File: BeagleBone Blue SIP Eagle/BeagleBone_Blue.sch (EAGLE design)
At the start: 278 parts, among them M1 JST_ZH_2, M2 JST_ZH_2, M3 JST_ZH_2, M4 JST_ZH_2, P10 SCHA5B0200, Q3 MOSFET-N, U1 TPD4S012_DRY_6, U4 TPD4S012_DRY_6, U5 24LC_32AT-I/OT, U6 SN74LVC1G07_DCK_5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

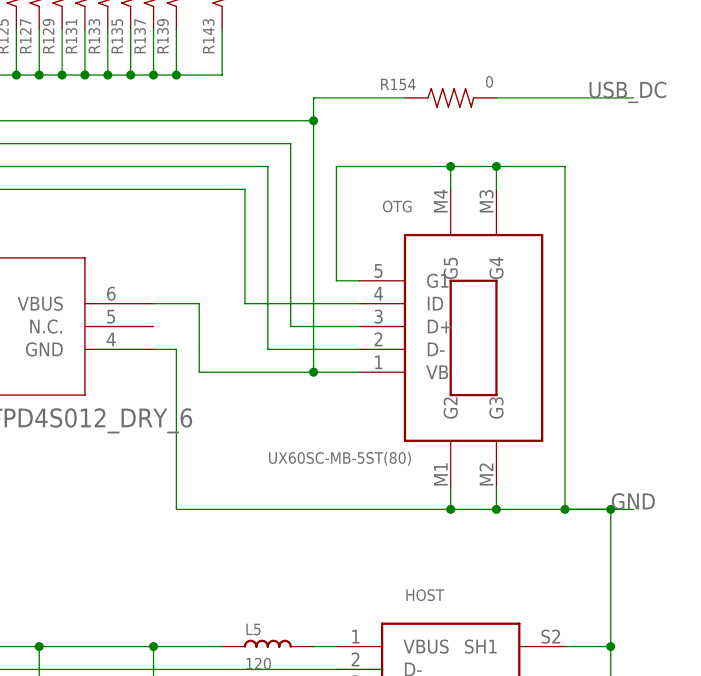
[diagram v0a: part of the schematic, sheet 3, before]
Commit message: swap to MicroUSB connector
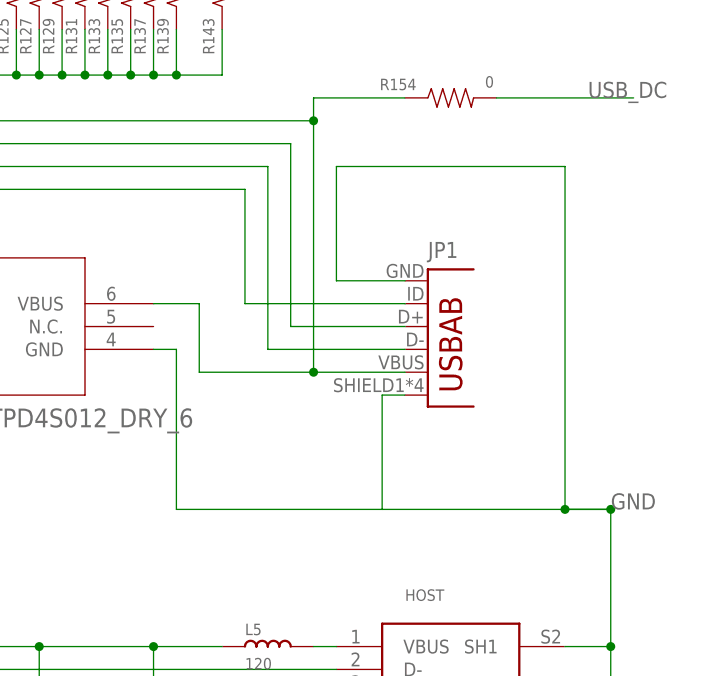
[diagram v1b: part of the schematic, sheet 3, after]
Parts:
- removed OTG: UX60SC-MB-5ST(80), BeagleBone_Blue:UX60SC-MB-5ST(80)
- added JP1: (no value), Strawson_Eagle_Lib:USB-AB
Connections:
- net GND: now also JP1.GND, JP1.SHIELD; no longer OTG.G1, OTG.G2, OTG.G3, OTG.G4, OTG.G5
- net N$117: now also JP1.D+; no longer OTG.D+
- net N$118: now also JP1.D-; no longer OTG.D-
- net N$119: now also JP1.USBID; no longer OTG.ID
- net USB0_VBUS: now also JP1.VBUS; no longer OTG.VB
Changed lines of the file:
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@@
 <part name="U4" library="BeagleBone_Blue" deviceset="TPD4S012_DRY_6" device=""/>
 <part name="U7" library="BeagleBone_Blue" deviceset="TPS2051B_D_8" device=""/>
-<part name="OTG" library="BeagleBone_Blue" deviceset="UX60SC-MB-5ST(80)" device=""/>
 <part name="HOST" library="BeagleBone_Blue" deviceset="87520-0010BLF" device=""/>
 <part name="R149" library="Strawson_Eagle_Lib" deviceset="RESISTOR" device="0402-RES" value="0"/>
@@
 <part name="R158" library="Strawson_Eagle_Lib" deviceset="RESISTOR" device="0402-RES" value="10K,1%"/>
 <part name="5VREG" library="BeagleBone_Blue" deviceset="AP1509" device="SOIC-8-TIGHT" value="AP1509SOIC-8-TIGHT"/>
+<part name="JP1" library="Strawson_Eagle_Lib" deviceset="USB-AB" device=""/>
 </parts>
 <sheets>
@@
 <instance part="U4" gate="A" x="228.6" y="68.58"/>
 <instance part="U7" gate="A" x="172.72" y="71.12"/>
-<instance part="OTG" gate="G$1" x="320.04" y="91.44" smashed="yes">
-<attribute name="NAME" x="317.5" y="116.84" size="1.27" layer="95"/>
-</instance>
 <instance part="HOST" gate="G$1" x="317.5" y="58.42"/>
 <instance part="R149" gate="G$1" x="203.2" y="127" smashed="yes">
@@
 </instance>
 <instance part="FRAME4" gate="G$1" x="0" y="0"/>
+<instance part="JP1" gate="G$1" x="325.12" y="104.14"/>
 </instances>
 <busses>
@@
 </segment>
 <segment>
-<pinref part="OTG" gate="G$1" pin="G2"/>
-<wire x1="325.12" y1="86.36" x2="325.12" y2="83.82" width="0.1524" layer="91"/>
-<wire x1="325.12" y1="83.82" x2="330.2" y2="83.82" width="0.1524" layer="91"/>
-<pinref part="OTG" gate="G$1" pin="G3"/>
-<wire x1="330.2" y1="83.82" x2="342.9" y2="83.82" width="0.1524" layer="91"/>
-<wire x1="330.2" y1="86.36" x2="330.2" y2="83.82" width="0.1524" layer="91"/>
-<junction x="330.2" y="83.82"/>
-<pinref part="OTG" gate="G$1" pin="G5"/>
-<wire x1="325.12" y1="119.38" x2="325.12" y2="121.92" width="0.1524" layer="91"/>
-<wire x1="325.12" y1="121.92" x2="330.2" y2="121.92" width="0.1524" layer="91"/>
-<wire x1="330.2" y1="121.92" x2="337.82" y2="121.92" width="0.1524" layer="91"/>
 <wire x1="337.82" y1="121.92" x2="337.82" y2="83.82" width="0.1524" layer="91"/>
-<pinref part="OTG" gate="G$1" pin="G4"/>
-<wire x1="330.2" y1="119.38" x2="330.2" y2="121.92" width="0.1524" layer="91"/>
-<junction x="330.2" y="121.92"/>
 <wire x1="337.82" y1="83.82" x2="342.9" y2="83.82" width="0.1524" layer="91"/>
 <junction x="337.82" y="83.82"/>
-<pinref part="OTG" gate="G$1" pin="G1"/>
-<wire x1="342.9" y1="83.82" x2="345.44" y2="83.82" width="0.1524" layer="91"/>
-<wire x1="314.96" y1="109.22" x2="312.42" y2="109.22" width="0.1524" layer="91"/>
 <wire x1="312.42" y1="109.22" x2="312.42" y2="121.92" width="0.1524" layer="91"/>
-<wire x1="312.42" y1="121.92" x2="325.12" y2="121.92" width="0.1524" layer="91"/>
-<junction x="325.12" y="121.92"/>
+<wire x1="312.42" y1="121.92" x2="337.82" y2="121.92" width="0.1524" layer="91"/>
 <label x="342.9" y="83.82" size="1.778" layer="95"/>
 <pinref part="U1" gate="A" pin="GND"/>
 <wire x1="292.1" y1="101.6" x2="294.64" y2="101.6" width="0.1524" layer="91"/>
 <wire x1="294.64" y1="101.6" x2="294.64" y2="83.82" width="0.1524" layer="91"/>
-<wire x1="294.64" y1="83.82" x2="325.12" y2="83.82" width="0.1524" layer="91"/>
-<junction x="325.12" y="83.82"/>
+<wire x1="294.64" y1="83.82" x2="317.5" y2="83.82" width="0.1524" layer="91"/>
+<wire x1="317.5" y1="83.82" x2="342.9" y2="83.82" width="0.1524" layer="91"/>
 <wire x1="342.9" y1="83.82" x2="342.9" y2="68.58" width="0.1524" layer="91"/>
 <junction x="342.9" y="83.82"/>
@@
 <pinref part="C46" gate="G$1" pin="2"/>
 <junction x="279.4" y="53.34"/>
+<pinref part="JP1" gate="G$1" pin="GND"/>
+<wire x1="320.04" y1="109.22" x2="312.42" y2="109.22" width="0.1524" layer="91"/>
+<pinref part="JP1" gate="G$1" pin="SHIELD"/>
+<wire x1="320.04" y1="96.52" x2="317.5" y2="96.52" width="0.1524" layer="91"/>
+<wire x1="317.5" y1="96.52" x2="317.5" y2="83.82" width="0.1524" layer="91"/>
 </segment>
 <segment>
@@
 <wire x1="307.34" y1="124.46" x2="307.34" y2="104.14" width="0.1524" layer="91"/>
 <junction x="238.76" y="124.46"/>
-<pinref part="OTG" gate="G$1" pin="D+"/>
-<wire x1="307.34" y1="104.14" x2="314.96" y2="104.14" width="0.1524" layer="91"/>
+<wire x1="307.34" y1="104.14" x2="320.04" y2="104.14" width="0.1524" layer="91"/>
+<pinref part="JP1" gate="G$1" pin="D+"/>
 </segment>
 </net>
@@
 <wire x1="304.8" y1="121.92" x2="304.8" y2="101.6" width="0.1524" layer="91"/>
 <junction x="236.22" y="121.92"/>
-<pinref part="OTG" gate="G$1" pin="D-"/>
-<wire x1="304.8" y1="101.6" x2="314.96" y2="101.6" width="0.1524" layer="91"/>
+<wire x1="304.8" y1="101.6" x2="320.04" y2="101.6" width="0.1524" layer="91"/>
+<pinref part="JP1" gate="G$1" pin="D-"/>
 </segment>
 </net>
@@
 <wire x1="302.26" y1="119.38" x2="302.26" y2="106.68" width="0.1524" layer="91"/>
 <junction x="231.14" y="119.38"/>
-<pinref part="OTG" gate="G$1" pin="ID"/>
-<wire x1="302.26" y1="106.68" x2="314.96" y2="106.68" width="0.1524" layer="91"/>
+<wire x1="302.26" y1="106.68" x2="320.04" y2="106.68" width="0.1524" layer="91"/>
+<pinref part="JP1" gate="G$1" pin="USBID"/>
 </segment>
 </net>
@@
 <wire x1="297.18" y1="106.68" x2="297.18" y2="99.06" width="0.1524" layer="91"/>
 <wire x1="297.18" y1="99.06" x2="309.88" y2="99.06" width="0.1524" layer="91"/>
-<pinref part="OTG" gate="G$1" pin="VB"/>
-<wire x1="309.88" y1="99.06" x2="314.96" y2="99.06" width="0.1524" layer="91"/>
 <junction x="309.88" y="99.06"/>
 <pinref part="R149" gate="G$1" pin="2"/>
@@
 <pinref part="R154" gate="G$1" pin="1"/>
 <wire x1="309.88" y1="129.54" x2="320.04" y2="129.54" width="0.1524" layer="91"/>
+<pinref part="JP1" gate="G$1" pin="VBUS"/>
+<wire x1="309.88" y1="99.06" x2="320.04" y2="99.06" width="0.1524" layer="91"/>
 </segment>
 </net>

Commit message: fix incorrect name and origin for usb host port and capacitor in library
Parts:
- renumbered C$1 to C50
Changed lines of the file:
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@@
 <part name="L5" library="Seeed-OPL-Inductor" deviceset="INDUCTOR/FERRITE-BEAD" device="'0603'" value="120"/>
 <part name="R156" library="Strawson_Eagle_Lib" deviceset="RESISTOR" device="0402-RES" value="33"/>
-<part name="C$1" library="BeagleBone_Blue" deviceset="AVE107M06D16T-F" device=""/>
+<part name="C50" library="BeagleBone_Blue" deviceset="AVE107M06D16T-F" device=""/>
 <part name="R157" library="Strawson_Eagle_Lib" deviceset="RESISTOR" device="0402-RES" value="10K,1%,DNI"/>
 <part name="C45" library="Strawson_Eagle_Lib" deviceset="CAP" device="0402-CAP" value="0.1UF,6.3V"/>
@@
 <attribute name="VALUE" x="209.55" y="110.998" size="1.27" layer="96" align="center-left"/>
 </instance>
-<instance part="C$1" gate="G$1" x="144.78" y="55.88"/>
+<instance part="C50" gate="G$1" x="144.78" y="55.88"/>
 <instance part="R157" gate="G$1" x="203.2" y="93.98" smashed="yes">
 <attribute name="NAME" x="199.39" y="95.4786" size="1.27" layer="95" align="center-right"/>
@@
 <pinref part="L4" gate="L" pin="1"/>
 <wire x1="297.18" y1="60.96" x2="299.72" y2="60.96" width="0.1524" layer="91"/>
-<pinref part="C$1" gate="G$1" pin="2"/>
+<pinref part="C50" gate="G$1" pin="2"/>
 <wire x1="144.78" y1="55.88" x2="144.78" y2="53.34" width="0.1524" layer="91"/>
 <wire x1="144.78" y1="53.34" x2="170.18" y2="53.34" width="0.1524" layer="91"/>
@@
 <junction x="152.4" y="68.58"/>
 <junction x="134.62" y="68.58"/>
-<pinref part="C$1" gate="G$1" pin="1"/>
+<pinref part="C50" gate="G$1" pin="1"/>
 <wire x1="144.78" y1="68.58" x2="144.78" y2="63.5" width="0.1524" layer="91"/>
 <junction x="144.78" y="68.58"/>

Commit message: new connector placement and screenshot
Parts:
- renumbered JP1 to USB
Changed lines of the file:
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@@
 <part name="R158" library="Strawson_Eagle_Lib" deviceset="RESISTOR" device="0402-RES" value="10K,1%"/>
 <part name="5VREG" library="BeagleBone_Blue" deviceset="AP1509" device="SOIC-8-TIGHT" value="AP1509SOIC-8-TIGHT"/>
-<part name="JP1" library="Strawson_Eagle_Lib" deviceset="USB-AB" device=""/>
+<part name="USB" library="Strawson_Eagle_Lib" deviceset="USB-AB" device=""/>
 </parts>
 <sheets>
@@
 </instance>
 <instance part="FRAME4" gate="G$1" x="0" y="0"/>
-<instance part="JP1" gate="G$1" x="325.12" y="104.14"/>
+<instance part="USB" gate="G$1" x="325.12" y="104.14"/>
 </instances>
 <busses>
@@
 <pinref part="C46" gate="G$1" pin="2"/>
 <junction x="279.4" y="53.34"/>
-<pinref part="JP1" gate="G$1" pin="GND"/>
+<pinref part="USB" gate="G$1" pin="GND"/>
 <wire x1="320.04" y1="109.22" x2="312.42" y2="109.22" width="0.1524" layer="91"/>
-<pinref part="JP1" gate="G$1" pin="SHIELD"/>
+<pinref part="USB" gate="G$1" pin="SHIELD"/>
 <wire x1="320.04" y1="96.52" x2="317.5" y2="96.52" width="0.1524" layer="91"/>
 <wire x1="317.5" y1="96.52" x2="317.5" y2="83.82" width="0.1524" layer="91"/>
@@
 <junction x="238.76" y="124.46"/>
 <wire x1="307.34" y1="104.14" x2="320.04" y2="104.14" width="0.1524" layer="91"/>
-<pinref part="JP1" gate="G$1" pin="D+"/>
+<pinref part="USB" gate="G$1" pin="D+"/>
 </segment>
 </net>
@@
 <junction x="236.22" y="121.92"/>
 <wire x1="304.8" y1="101.6" x2="320.04" y2="101.6" width="0.1524" layer="91"/>
-<pinref part="JP1" gate="G$1" pin="D-"/>
+<pinref part="USB" gate="G$1" pin="D-"/>
 </segment>
 </net>
@@
 <junction x="231.14" y="119.38"/>
 <wire x1="302.26" y1="106.68" x2="320.04" y2="106.68" width="0.1524" layer="91"/>
-<pinref part="JP1" gate="G$1" pin="USBID"/>
+<pinref part="USB" gate="G$1" pin="USBID"/>
 </segment>
 </net>
@@
 <pinref part="R154" gate="G$1" pin="1"/>
 <wire x1="309.88" y1="129.54" x2="320.04" y2="129.54" width="0.1524" layer="91"/>
-<pinref part="JP1" gate="G$1" pin="VBUS"/>
+<pinref part="USB" gate="G$1" pin="VBUS"/>
 <wire x1="309.88" y1="99.06" x2="320.04" y2="99.06" width="0.1524" layer="91"/>
 </segment>
